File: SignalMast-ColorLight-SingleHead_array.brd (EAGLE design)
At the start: 103.6 x 103.5 mm, 49 parts

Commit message: added missing values
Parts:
- BOARD1: value (none) -> 10x10
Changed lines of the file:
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@@
 </autorouter>
 <elements>
-<element name="BOARD1" library="SPCoast" package="BOARD-SEEED10X10-NOHOLES" value="" x="0" y="0"/>
+<element name="BOARD1" library="SPCoast" package="BOARD-SEEED10X10-NOHOLES" value="10x10" x="0" y="0"/>
 <element name="GYR+" library="SPCoast" package="1X04_LOCK" value="CONNECTOR-GROVE-4P-2.0-3470130P1" x="22.86" y="5.08" smashed="yes" rot="R180">
 <attribute name="NAME" x="15.621" y="0.762" size="1.778" layer="25" font="vector" ratio="11" rot="SR0"/>

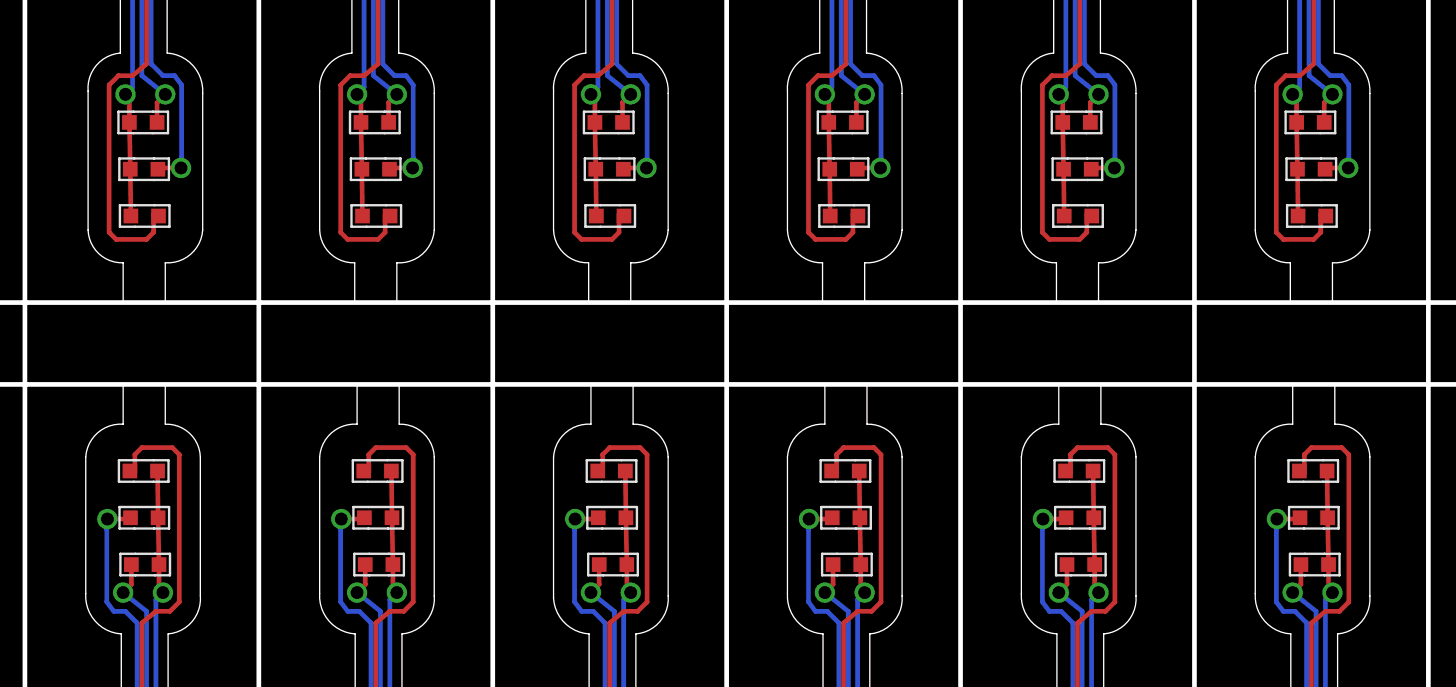
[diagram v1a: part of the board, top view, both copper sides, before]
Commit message: normalized values
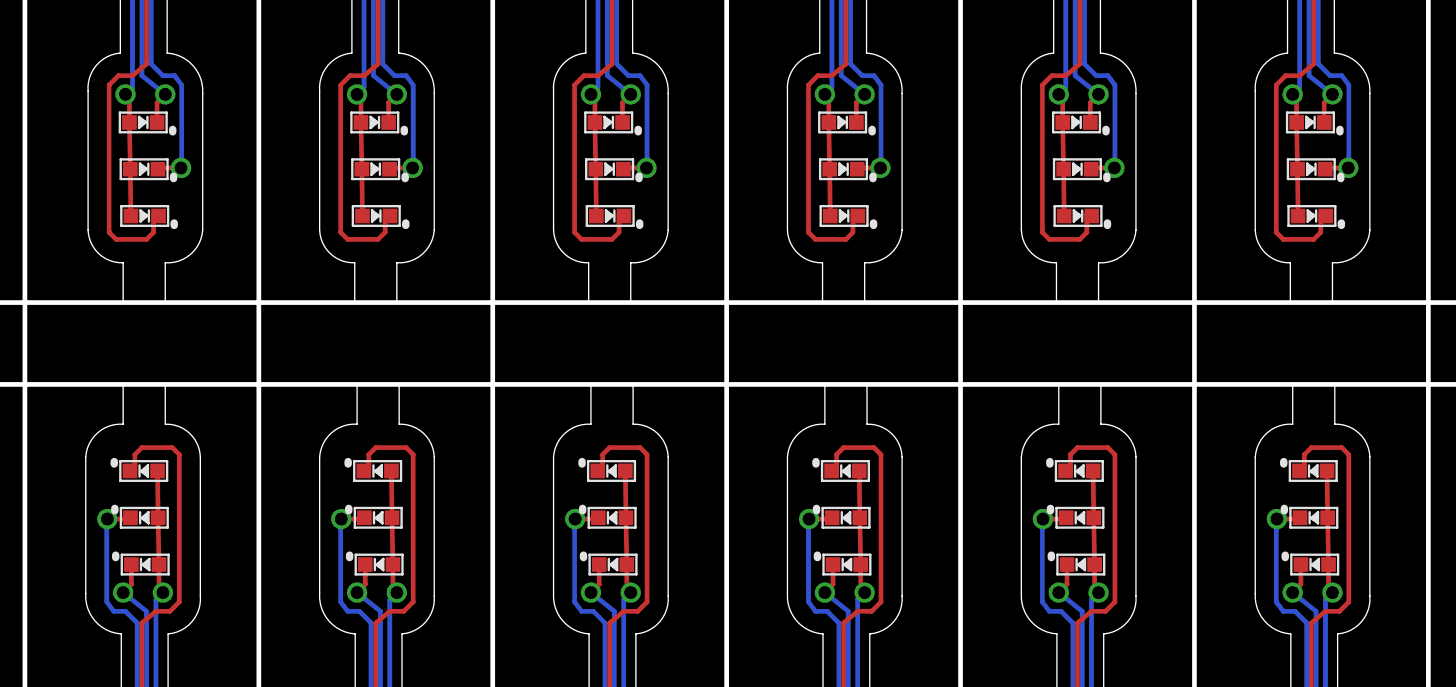
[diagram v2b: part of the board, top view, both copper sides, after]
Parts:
- BOARD1: value 10x10 -> BOARD
- GYR+, GYR+1, GYR+10, GYR+11, GYR+2, GYR+3, GYR+4, GYR+5, GYR+6, GYR+7, GYR+8, GYR+9: value CONNECTOR-GROVE-4P-2.0-3470130P1 -> 0.100
- turned LED1 to 0 degrees
- turned LED10 to 0 degrees
- turned LED11 to 0 degrees
- turned LED12 to 0 degrees
- turned LED13 to 0 degrees
- turned LED14 to 0 degrees
- turned LED15 to 0 degrees
- turned LED16 to 0 degrees
- turned LED17 to 0 degrees
- turned LED18 to 0 degrees
- turned LED19 to 180 degrees
- turned LED2 to 0 degrees
- turned LED20 to 180 degrees
- turned LED21 to 180 degrees
- turned LED22 to 180 degrees
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
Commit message: Version 1.3
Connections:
- net BR7: no longer GYR+7.2
- net BY6: no longer GYR+6.3
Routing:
- net BY6: track 38.7 -> 36.6 mm
- net BR7: track 34.6 -> 34.0 mm
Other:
- board text added: "2020-10"
- board text added: "G Y R +"
- board text removed: "GYR+"
- board text removed: "V1.0D"
